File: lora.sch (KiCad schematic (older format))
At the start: 64 parts, among them J1 Conn_01x02, J11 Conn_Coaxial, J2 Humidity, J3 Temp, J4 Programming_Jumper, J5 Temp, J6 VDD, J7 GPS, J8 SIM800, J9 I2C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

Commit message: almost done.. more work than expected to change the connector position and size
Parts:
- removed H2: MountingHole_Pad, MountingHole:MountingHole_2.2mm_M2_DIN965_Pad, symbol Mechanical:MountingHole_Pad
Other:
- moved on the sheet: H3
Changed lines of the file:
@@
 $EndComp
 $Comp
-L Mechanical:MountingHole_Pad H2
-U 1 1 5FEA1D5A
+L Mechanical:MountingHole_Pad H3
+U 1 1 5FED213B
 P 2375 4425
-F 0 "H2" H 2475 4474 50  0000 L CNN
+F 0 "H3" H 2475 4474 50  0000 L CNN
 F 1 "MountingHole_Pad" H 2475 4383 50  0000 L CNN
 F 2 "MountingHole:MountingHole_2.2mm_M2_DIN965_Pad" H 2375 4425 50  0001 C CNN
@@
 $EndComp
 $Comp
-L power:GND #PWR04
-U 1 1 5FEA1D60
+L power:GND #PWR05
+U 1 1 5FED2141
 P 2375 4525
-F 0 "#PWR04" H 2375 4275 50  0001 C CNN
+F 0 "#PWR05" H 2375 4275 50  0001 C CNN
 F 1 "GND" H 2380 4352 50  0000 C CNN
 F 2 "" H 2375 4525 50  0001 C CNN
@@
 	1    0    0    -1
 $EndComp
-$Comp
-L Mechanical:MountingHole_Pad H3
-U 1 1 5FED213B
-P 2375 4925
-F 0 "H3" H 2475 4974 50  0000 L CNN
-F 1 "MountingHole_Pad" H 2475 4883 50  0000 L CNN
-F 2 "MountingHole:MountingHole_2.2mm_M2_DIN965_Pad" H 2375 4925 50  0001 C CNN
-F 3 "~" H 2375 4925 50  0001 C CNN
-	1    2375 4925
-	1    0    0    -1
-$EndComp
-$Comp
-L power:GND #PWR05
-U 1 1 5FED2141
-P 2375 5025
-F 0 "#PWR05" H 2375 4775 50  0001 C CNN
-F 1 "GND" H 2380 4852 50  0000 C CNN
-F 2 "" H 2375 5025 50  0001 C CNN
-F 3 "" H 2375 5025 50  0001 C CNN
-	1    2375 5025
-	1    0    0    -1
-$EndComp

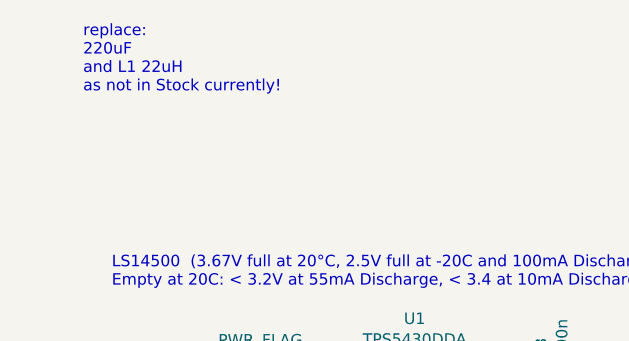
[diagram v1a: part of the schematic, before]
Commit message: finalized design and exchanges 220u capacity with a one in stock.
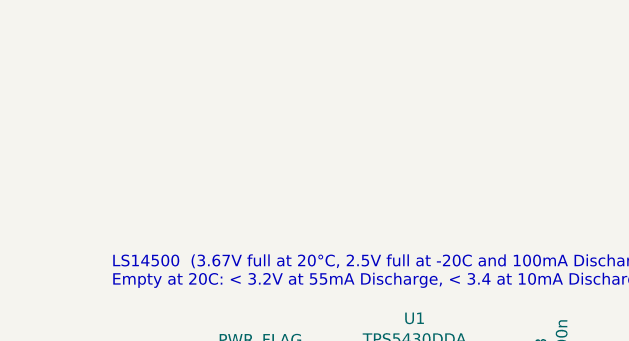
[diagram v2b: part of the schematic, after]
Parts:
- C4: LCSC C127327 -> C127968
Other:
- note removed: "replace:\n220uF \nand L1 22uH \nas not in Stock currently!"
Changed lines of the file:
@@
 F 2 "Capacitor_SMD:CP_Elec_6.3x7.7" H 3413 1100 50  0001 C CNN
 F 3 "~" H 3375 1250 50  0001 C CNN
-F 4 "C127327" H 3375 1250 50  0001 C CNN "LCSC"
+F 4 "C127968" H 3375 1250 50  0001 C CNN "LCSC"
 	1    3375 1250
 	1    0    0    -1
@@
 	1    0    0    -1
 $EndComp
-Text Notes 625  -150 0    50   ~ 0
-replace:\n220uF \nand L1 22uH    \nas not in Stock currently!
 $EndSCHEMATC

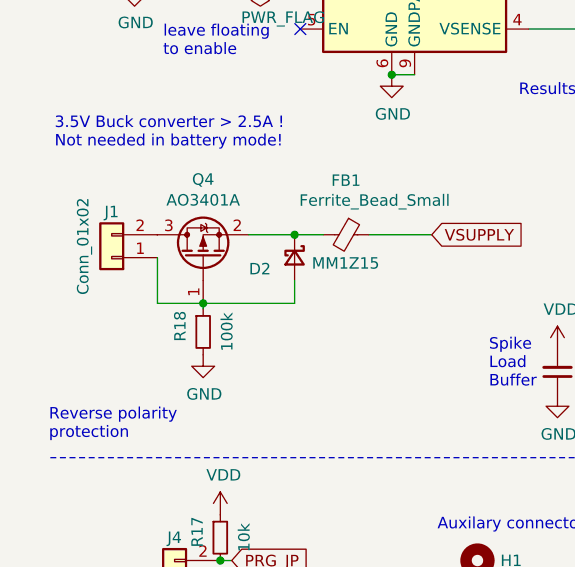
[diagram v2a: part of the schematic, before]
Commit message: corrected GND on input terminal
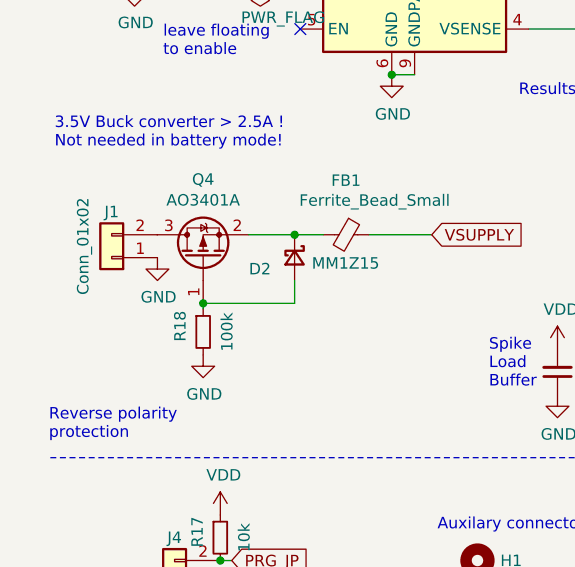
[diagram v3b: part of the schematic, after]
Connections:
- net GND: now also J1.1 (Pin_1)
- net at D2.2 (A), Q4.1 (G), R18.1: no longer J1.1 (Pin_1)
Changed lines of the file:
@@
 	1    0    0    -1
 $EndComp
-Text Notes 750  700  0    50   ~ 0
-LS14500  (3.67V full at 20°C, 2.5V full at -20C and 100mA Discharge)\nEmpty at 20C: < 3.2V at 55mA Discharge, < 3.4 at 10mA Discharge)
 $Comp
 L Switch:SW_MEC_5E SW1
@@
 Text GLabel 2150 2400 2    50   Input ~ 0
 VSUPPLY
-Wire Wire Line
-	1150 2700 950  2700
-Wire Wire Line
-	950  2700 950  2500
 Wire Wire Line
 	2525 7350 1600 7350
@@
 	1    0    0    -1
 $EndComp
+Text Notes 750  700  0    50   ~ 0
+LS14500  (3.67V full at 20°C, 2.5V full at -20C and 100mA Discharge)\nEmpty at 20C: < 3.2V at 55mA Discharge, < 3.4 at 10mA Discharge)
+$Comp
+L power:GND #PWR?
+U 1 1 6137C0D3
+P 950 2500
+F 0 "#PWR?" H 950 2250 50  0001 C CNN
+F 1 "GND" H 955 2327 50  0000 C CNN
+F 2 "" H 950 2500 50  0001 C CNN
+F 3 "" H 950 2500 50  0001 C CNN
+	1    950  2500
+	1    0    0    -1
+$EndComp

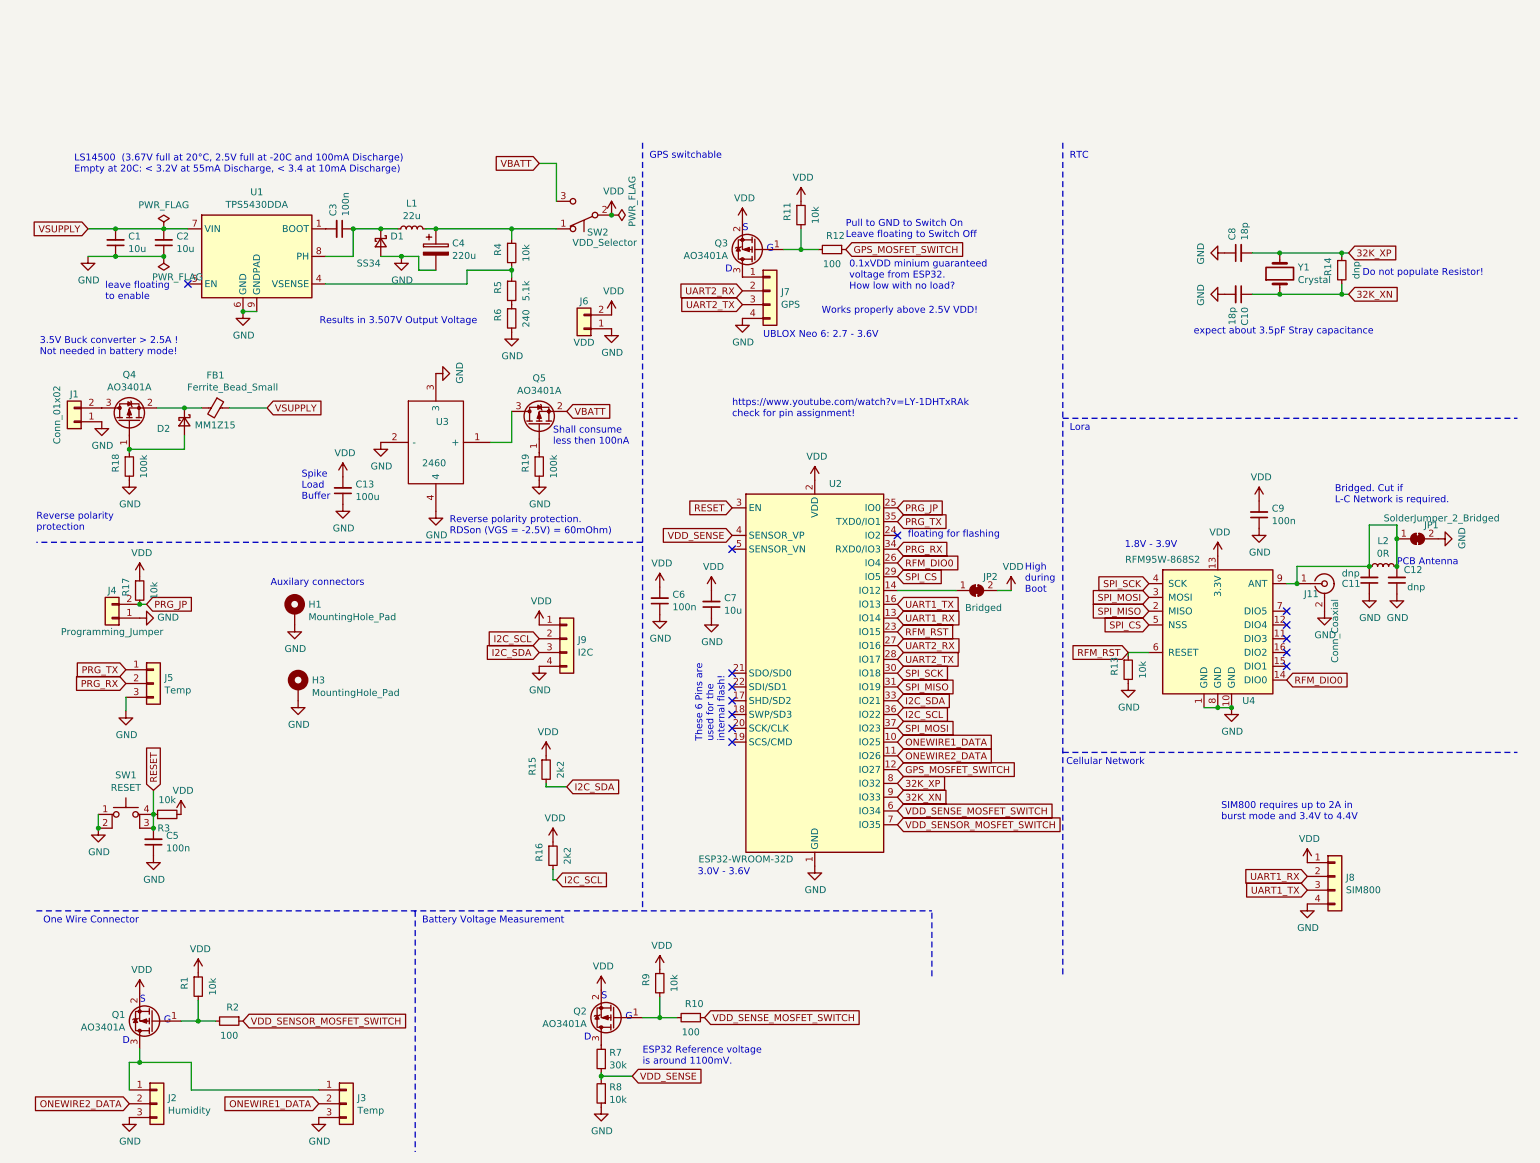
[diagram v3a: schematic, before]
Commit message: remove rfm reset pulldown, add spi pullups, switch for programming added, labels backside added
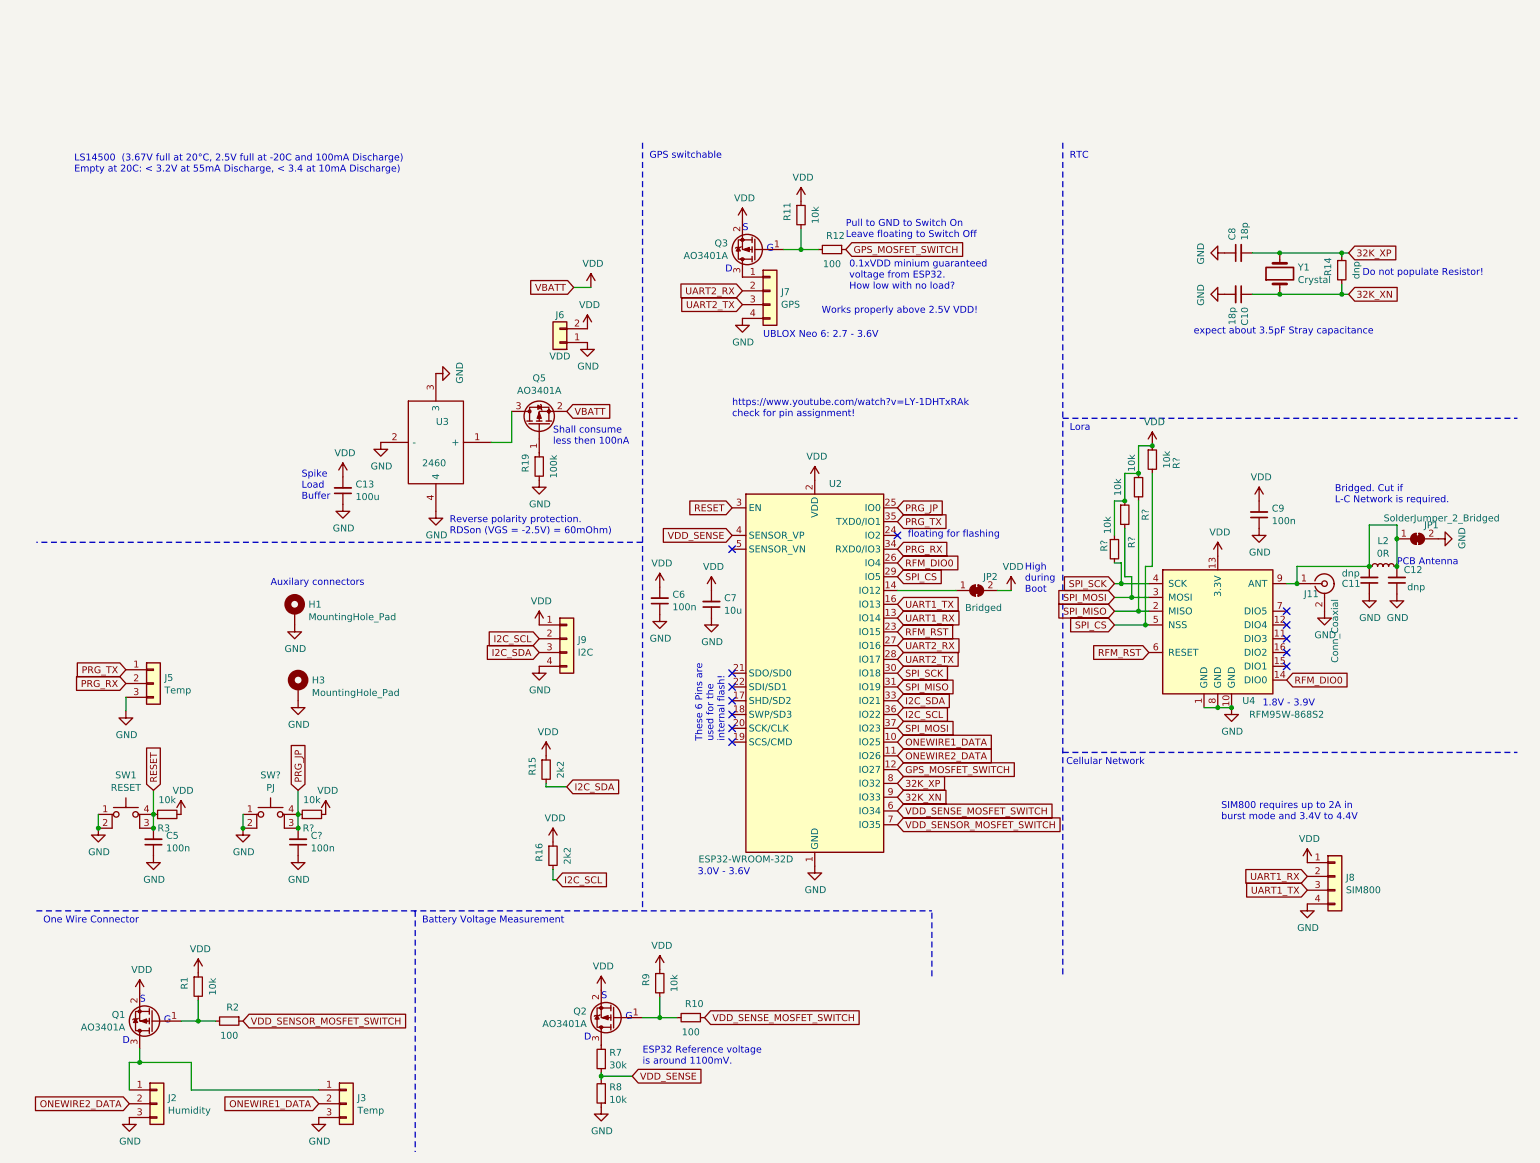
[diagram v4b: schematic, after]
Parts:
- removed C1, C2: 10u, Capacitor_SMD:C_1206_3216Metric, symbol Device:C_Small
- removed C3: 100n, Capacitor_SMD:C_0603_1608Metric, symbol Device:C_Small
- removed C4: 220u, Capacitor_SMD:CP_Elec_6.3x7.7, symbol Device:CP
- removed D1: SS34, Diode_SMD:D_SMA, symbol Device:D_Schottky_Small
- removed D2: MM1Z15, Diode_SMD:D_SOD-123, symbol Device:D_Schottky_Small
- removed FB1: Ferrite_Bead_Small, Resistor_SMD:R_0805_2012Metric, symbol Device:Ferrite_Bead_Small
- removed J1: Conn_01x02, Connector_PinHeader_2.54mm:PinHeader_1x02_P2.54mm_Horizontal, symbol Connector_Generic:Conn_01x02
- removed J4: Programming_Jumper, Connector_PinHeader_2.54mm:PinHeader_1x02_P2.54mm_Vertical, symbol Connector_Generic:Conn_01x02
- removed L1: 22u, OWN_Parts_:L_MS1040-220M, symbol Device:L_Small
- removed Q4: AO3401A, Package_TO_SOT_SMD:SOT-23, symbol Transistor_FET:AO3401A
- removed R13, R17, R4: 10k, Capacitor_SMD:C_0603_1608Metric, symbol Device:R_Small
- removed R18: 100k, Resistor_SMD:R_0603_1608Metric, symbol Device:R_Small
- removed R5: 5.1k, Resistor_SMD:R_0603_1608Metric, symbol Device:R_Small
- removed R6: 240, Resistor_SMD:R_0603_1608Metric, symbol Device:R_Small
- removed SW2: VDD_Selector, Connector_PinHeader_2.54mm:PinHeader_1x03_P2.54mm_Vertical, symbol Switch:SW_Push_SPDT
- removed U1: TPS5430DDA, Package_SO:TI_SO-PowerPAD-8_ThermalVias, symbol Regulator_Switching:TPS5430DDA
- added C?: 100n, Capacitor_SMD:C_0603_1608Metric, symbol Device:C_Small
- added R? (x5): 10k, Capacitor_SMD:C_0603_1608Metric, symbol Device:R_Small
- added SW?: PJ, OWN_Parts_:TS-1187A-C-E-B, symbol Switch:SW_MEC_5E
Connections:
- net VBATT is gone; now on net VDD: Q5.2 (S)
- net GND: now also C?.1, SW?.1, SW?.2
- net PRG_JP: now also C?.2, R?.1, SW?.3 (K), SW?.4 (A)
- net SPI_CS: now also R?.2
- net SPI_MISO: now also R?.2
- net SPI_MOSI: now also R?.2
- net SPI_SCK: now also R?.2
- net VDD: now also R?.1, R?.1, R?.1, R?.1, R?.2
- no-connect marks 14 -> 13
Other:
- note removed: "3.5V Buck converter > 2.5A !\nNot needed in battery mode!"
- note removed: "Results in 3.507V Output Voltage"
- note removed: "Reverse polarity \nprotection"
- note removed: "leave floating\nto enable"
- moved on the sheet: J6
